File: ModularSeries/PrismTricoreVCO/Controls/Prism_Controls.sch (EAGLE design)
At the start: 10 parts

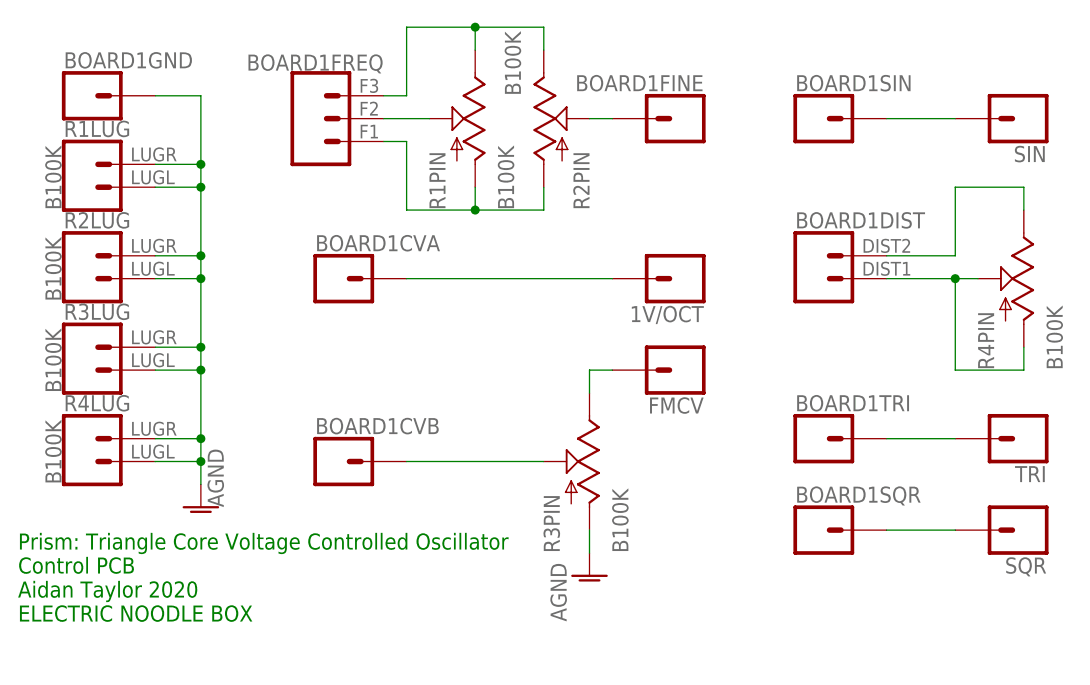
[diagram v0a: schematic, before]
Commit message: Prism control card updated to accomodate Cinch nanas
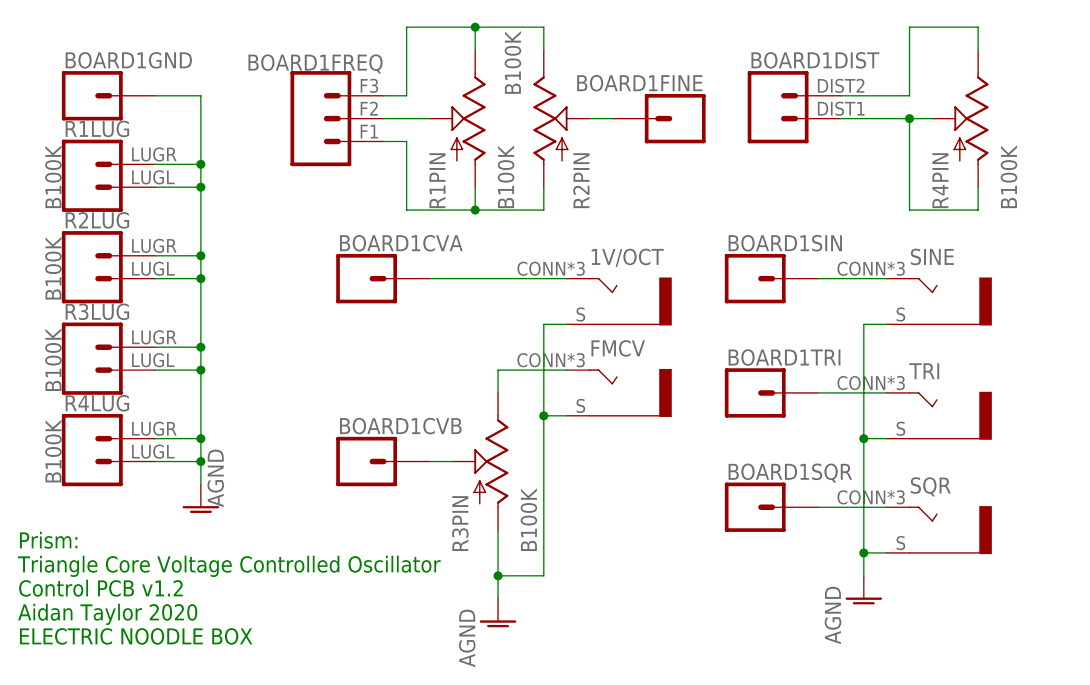
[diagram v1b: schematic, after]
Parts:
- removed SIN: BANANA_PANEL, ElectricNoodleBox:BANANA_PANEL
- added SINE: COMBI-JACKCINCHNANA, ElectricNoodleBox:COMBI-JACKCINCHNANA
- 1V/OCT, FMCV, SQR, TRI: value BANANA_PANEL -> COMBI-JACKCINCHNANA; device ElectricNoodleBox:BANANA_PANEL -> ElectricNoodleBox:COMBI-JACKCINCHNANA
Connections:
- net AGND: now also 1V/OCT.S, FMCV.S, SINE.S, SQR.S, TRI.S
- net N$1: now also 1V/OCT.T; no longer 1V/OCT.1
- net N$10: now also SINE.T; no longer SIN.1
- net N$11: now also TRI.T; no longer TRI.1
- net N$12: now also SQR.T; no longer SQR.1
- net N$6: now also FMCV.T; no longer FMCV.1
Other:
- note added: "Prism: Triangle Core Voltage Controlled Oscillator Control PCB v1.2 Aidan Taylor 2020 ELECTRIC NOODLE BOX"
- note removed: "Prism: Triangle Core Voltage Controlled Oscillator Control PCB Aidan Taylor 2020 ELECTRIC NOODLE BOX"
- moved on the sheet: BOARD1CVA, BOARD1CVB, BOARD1DIST, BOARD1SIN, BOARD1SQR, BOARD1TRI, R3PIN, R4PIN
